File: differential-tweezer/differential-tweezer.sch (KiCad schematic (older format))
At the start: 58 parts, among them J1 5V, J2 IN+, J3 Conn_Coaxial, J4 IN-, J5 Power, U1 R1283B, U2 OPA810, U3 OPA810, U4 OPA810

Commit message: Revision 2
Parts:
- removed C11, C3: 100nF, Capacitor_SMD:C_0603_1608Metric, symbol Device:C
- removed C19: 2pF, Capacitor_SMD:C_0603_1608Metric, symbol Device:C
- removed C23: 6pF, Capacitor_SMD:C_Trimmer_Murata_TZC3, symbol Device:CTRIM
- removed J1: 5V, oscilloscope-probes:WIREPAD_WIDE, symbol Connector:Conn_01x01_Female
- removed J2: IN+, oscilloscope-probes:SOLDERPAD_3x1.5, symbol Connector:Conn_01x01_Female
- removed J3: Conn_Coaxial, oscilloscope-probes:COAX_SOLDER, symbol Connector:Conn_Coaxial
- removed J4: IN-, oscilloscope-probes:SOLDERPAD_3x1.5, symbol Connector:Conn_01x01_Female
- removed J5: Power, Connector_PinHeader_2.54mm:PinHeader_1x04_P2.54mm_Vertical, symbol Connector:Conn_01x04_Male
- removed L3, L5: 1k, Inductor_SMD:L_0603_1608Metric, symbol Device:L_Core_Ferrite
- removed RV1, RV3: 47k, Potentiometer_SMD:Potentiometer_Bourns_TC33X_Vertical, symbol Device:R_POT_TRIM
- removed U2, U3, U4: OPA810, Package_TO_SOT_SMD:SOT-23-5, symbol Amplifier_Operational:OPA842xDBV
- added C1, C26: 10µF, Capacitor_SMD:C_0603_1608Metric, symbol Device:C
- added C10: 100nF, Capacitor_SMD:C_0603_1608Metric, symbol Device:C
- added C14, C15: 20pF, Capacitor_SMD:C_0603_1608Metric, symbol Device:C
- added H1: 2.2mm, MountingHole:MountingHole_2.2mm_M2_DIN965_Pad, symbol Mechanical:MountingHole_Pad
- added J1: Triax, oscilloscope-probes:TRIAX_TUBE, symbol oscilloscope_probes:Conn_Triaxial
- added J2: Input, oscilloscope-probes:Tensility_54-00177, symbol Connector:AudioJack4
- added J3: Probe+, oscilloscope-probes:TE_2306454_RIGHT, symbol Connector_Generic:Conn_01x01
- added J4: Probe+_GND, oscilloscope-probes:TE_2306454_RIGHT, symbol Connector_Generic:Conn_01x01
- added J5: Probe-_GND, oscilloscope-probes:TE_2306454_LEFT, symbol Connector_Generic:Conn_01x01
- added J6: Probe-, oscilloscope-probes:TE_2306454_LEFT, symbol Connector_Generic:Conn_01x01
- added L1, L7, L8: MMZ1608B601, Inductor_SMD:L_0603_1608Metric, symbol Device:L_Core_Ferrite
- added R14, R15: 220, Resistor_SMD:R_0603_1608Metric, symbol Device:R
- added R16, R17: 22, Resistor_SMD:R_0603_1608Metric, symbol Device:R
- added R7: 10M, Resistor_SMD:R_0603_1608Metric, symbol Device:R
- added R9: 499k, Resistor_SMD:R_0603_1608Metric, symbol Device:R
- added RV2: 50k, Potentiometer_SMD:Potentiometer_Bourns_TC33X_Vertical, symbol Device:R_POT_TRIM
- added SW1: GAIN, oscilloscope-probes:78HF01GWRT, symbol Switch:SW_SPST
- added TP1: +5V, TestPoint:TestPoint_Pad_D2.5mm, symbol Connector:TestPoint
- added TP2: +6V, TestPoint:TestPoint_Pad_D2.5mm, symbol Connector:TestPoint
- added TP3: -6V, TestPoint:TestPoint_Pad_D2.5mm, symbol Connector:TestPoint
- added TP4: GND, TestPoint:TestPoint_Pad_D2.5mm, symbol Connector:TestPoint
- added U2, U3, U4: OPA659, Package_SON:Texas_S-PVSON-N8_ThermalVias, symbol oscilloscope_probes:OPA659DRB
- C12: renamed from C4; footprint Capacitor_SMD:C_0805_2012Metric -> Capacitor_SMD:C_0603_1608Metric; Mfg (none) -> AVX; Mfg Part No (none) -> 0603ZD106KAT2A; Notes (none) -> X5R, 10V
- C13: renamed from C12; footprint Capacitor_SMD:C_0805_2012Metric -> Capacitor_SMD:C_0603_1608Metric; Mfg (none) -> AVX; Mfg Part No (none) -> 0603ZD106KAT2A; Notes (none) -> X5R, 10V
- C16: renamed from C20; value 6pF -> 8-30pF; Mfg (none) -> EW; Mfg Part No (none) -> SGC3S300NM
- C17: renamed from C22; value 6pF -> 8-30pF; Mfg (none) -> EW; Mfg Part No (none) -> SGC3S300NM
- C19: renamed from C21; value 2pF -> N/A
- C2: renamed from C16; footprint Capacitor_SMD:C_0805_2012Metric -> Capacitor_SMD:C_0603_1608Metric; Mfg (none) -> AVX; Mfg Part No (none) -> 0603ZD106KAT2A; Notes (none) -> X5R, 10V
- C3: renamed from C17; footprint Capacitor_SMD:C_0805_2012Metric -> Capacitor_SMD:C_0603_1608Metric; Mfg (none) -> AVX; Mfg Part No (none) -> 0603ZD106KAT2A; Notes (none) -> X5R, 10V
- C4: renamed from C8; value 22nF -> 100pF; Mfg (none) -> Stackpole; Mfg Part No (none) -> CML0603C0G101JT50V; Notes (none) -> NP0
- C5: renamed from C18; value 22nF -> 100pF; Mfg (none) -> Stackpole; Mfg Part No (none) -> CML0603C0G101JT50V; Notes (none) -> NP0
- C6: renamed from C1; footprint Capacitor_SMD:C_0805_2012Metric -> Capacitor_SMD:C_0603_1608Metric; Mfg (none) -> AVX; Mfg Part No (none) -> 0603ZD106KAT2A; Notes (none) -> X5R, 10V
- C7: renamed from C9; footprint Capacitor_SMD:C_0805_2012Metric -> Capacitor_SMD:C_0603_1608Metric; Mfg (none) -> AVX; Mfg Part No (none) -> 0603ZD106KAT2A; Notes (none) -> X5R, 10V
- C8: renamed from C2; footprint Capacitor_SMD:C_0805_2012Metric -> Capacitor_SMD:C_0603_1608Metric; Mfg (none) -> AVX; Mfg Part No (none) -> 0603ZD106KAT2A; Notes (none) -> X5R, 10V
- C9: renamed from C10; footprint Capacitor_SMD:C_0805_2012Metric -> Capacitor_SMD:C_0603_1608Metric; Mfg (none) -> AVX; Mfg Part No (none) -> 0603ZD106KAT2A; Notes (none) -> X5R, 10V
- D1: renamed from D2; value BAT54 -> NSR05T30; footprint Diode_SMD:D_SOD-123 -> Diode_SMD:D_SOD-523; Mfg (none) -> ON; Mfg Part No (none) -> NSR05T30XV2T5G
- D2: renamed from D1; value BAT54 -> NSR05T30; footprint Diode_SMD:D_SOD-123 -> Diode_SMD:D_SOD-523; Mfg (none) -> ON; Mfg Part No (none) -> NSR05T30XV2T5G
- L2: renamed from L1; value 1k -> MMZ1608B601; Mfg (none) -> TDK; Mfg Part No (none) -> MMZ1608B601CTAH0; Notes (none) -> Alternative MMZ1608B471
- L3: renamed from L2; value 47µH -> 4.7µH; footprint Inductor_SMD:L_Taiyo-Yuden_NR-40xx_HandSoldering -> Inductor_SMD:L_0805_2012Metric
- L4: renamed from L7; value 47µH -> 4.7µH; footprint Inductor_SMD:L_Taiyo-Yuden_NR-40xx_HandSoldering -> Inductor_SMD:L_0805_2012Metric
- L5: renamed from L4; value 1k -> MMZ1608B601; Mfg (none) -> TDK; Mfg Part No (none) -> MMZ1608B601CTAH0; Notes (none) -> Alternative MMZ1608B471
- L6: value 1k -> MMZ1608B601; Mfg (none) -> TDK; Mfg Part No (none) -> MMZ1608B601CTAH0; Notes (none) -> Alternative MMZ1608B471
- R1: renamed from R6; value 10k -> 1k
- R10: value 1M -> 499k
- R12: renamed from R9; value 1M -> 475k
- R13: renamed from R15; value 1M -> 475k
- R18: renamed from R7; value 470 -> 110
- R19: renamed from R13; value 470 -> 110
- R2: value 100k -> 4.99k
- R20: renamed from R8; value 470 -> 220
- R21: renamed from R14; value 470 -> 220
- R22: renamed from R12; value 47 -> 49.9
- R3: renamed from R5; value 100k -> 4.99k
- R6: renamed from R3; value 10k -> 1k
- RV1: renamed from RV2; value 47k -> 50k; Mfg (none) -> Bourns; Mfg Part No (none) -> TC33X-2-503E
- renumbered C5 to C20, C13 to C21, C6 to C22, C14 to C23, C7 to C24, C15 to C25, R1 to R4, R4 to R5
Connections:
- net GND: now also C1.2, C10.2, C26.2, H1.1, J1.2 (Ext), J2.R2, J2.S, J4.1 (Pin_1), J5.1 (Pin_1), TP4.1; no longer RV1.3
- net IN+: now reaches C16.1, R12.1
- net IN+: now also C14.1, J3.1 (Pin_1), R9.1, U2.3 (+)
- net at R12.2, RV1.1: now also R7.2
- net IN-: now reaches C17.1, R13.1
- net IN-: now also R10.1, C15.1, J6.1 (Pin_1), U3.3 (+)
- net at R13.2: now also RV1.3
- net at R19.1: now also R15.2, U3.6
- net at C19.2, R19.2, R21.1: now also U4.2 (-)
- net at R18.1: now also R14.1, U2.6
- net at R18.2, R20.1: now also U4.3 (+)
- net at C19.1, R21.2, R22.2: now also U4.6
- net CONN_IN-: now reaches R10.2
- net CONN_IN-: now also C15.2, J2.R1; no longer R22.1
- net at C3.1, L2.2, L3.1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: now also C26.1
- net at C6.1, D2.1 (K), R2.1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: now also L5.1
- net at C7.1, D1.2 (A), R3.1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: now also L6.1
- net at C2.1, L2.1: now also L1.2
- net at C9.1: now also L6.2, L8.1; no longer L6.1
- net at C8.1: now also L5.2, L7.1; no longer L5.1
- net +12V renamed +6V
- net +6V: now also L7.2, RV2.1, TP2.1, U2.7 (V+), U3.7 (V+), U4.7 (V+); no longer L5.2
- net -12V renamed -6V
- net -6V: now also L8.2, RV2.3, TP3.1, U2.4 (V-), U2.9 (EP), U3.4 (V-), U3.9 (EP), U4.4 (V-), U4.9 (EP); no longer L6.2
- new net: R15.1, R17.2, U3.2 (-)
- new net: R14.2, R16.2, U2.2 (-)
- new net: R17.1, SW1.1 (A)
- new net: R16.1, SW1.2 (B)
- new net +5V: C1.1, J1.3, L1.1, TP1.1
- new net CONN_IN+: C14.2, J2.T, R9.2
- new net OFFSET_TRIM: C10.1, R7.1, RV2.2
- new net OUT: J1.1 (In), R22.1
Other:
- note added: "C16 and C17 trim input divider compensation.\nRV1 trims low-frequency CMRR.\nRV2 trims input offset voltage."
- note added: "Input has divider resistor and capacitor near the tip to minimize\ncapacitance. For 10x tweezers this is 9.53 Mohm || 1.2 pF.\nThe 3.5 mm input has 1 Mohm || 10 pF input impedance, while\ntweezer connector has 500 kohm || 20 pF."
- note added: "Input protection: OPA659 internal ESD diodes tolerate\nup to 30 mA current. The input divider provides enough\nprotection for any inputs up to the resistor maximum\nvoltage (100 V). The capacitive divider limits ESD events\nto below the 4kV HBM rating of OPA659."
- note added: "Input stage has switchable 1x or 10x amplification.\n\nOutput differential amplifier has 2x amplification ratio.\nR18-R21 should have low thermal drift for good CMMR."
- note removed: "Circuit can be assembled either on 1 PCB with 2-sided SMT,\nor 2 PCBs each with 1-sided SMT."
- note removed: "Probe tip has 9.1Mohm // 0.5pF.\nCombined this forms a 1:10 divider"
- moved on the sheet: C12, C13, C16, C17, C19, C2, C20, C21, C22, C23, C24, C25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

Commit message: Revision 3
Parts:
- removed C14, C15: 20pF, Capacitor_SMD:C_0603_1608Metric, symbol Device:C
- removed J1: Triax, oscilloscope-probes:TRIAX_TUBE, symbol oscilloscope_probes:Conn_Triaxial
- removed J2: Input, oscilloscope-probes:Tensility_54-00177, symbol Connector:AudioJack4
- removed R4, R5: 1k, Resistor_SMD:R_0603_1608Metric, symbol Device:R
- added C11: 3pF, Capacitor_SMD:C_0603_1608Metric, symbol Device:C
- added D3: RED, LED_SMD:LED_0603_1608Metric, symbol Device:LED_ALT
- added D4, D5, D6: PESD5V0X1B, Package_TO_SOT_SMD:SOT-23, symbol Device:D_Zener_x2_ACom_KKA
- added J1: Triax_inner, oscilloscope-probes:COAX_2MM, symbol Connector:Conn_Coaxial
- added J2: Triax_outer, oscilloscope-probes:TRIAX_OUTER_3MM, symbol Connector_Generic:Conn_01x01
- added J7: IN+, oscilloscope-probes:RF11-27A-T-00-50-G, symbol Connector:Conn_Coaxial
- added J8: IN-, oscilloscope-probes:RF11-27A-T-00-50-G, symbol Connector:Conn_Coaxial
- added L9: MMZ1608B601, Inductor_SMD:L_0603_1608Metric, symbol Device:L_Core_Ferrite
- added R11, R23: 110, Resistor_SMD:R_0603_1608Metric, symbol Device:R
- added R8: 5.1k, Resistor_SMD:R_0603_1608Metric, symbol Device:R
- C1: value 10µF -> 3pF
- C19: value N/A -> 3pF
- J3: value Probe+ -> Spring+S
- J4: value Probe+_GND -> Spring+G
- J5: value Probe-_GND -> Spring-G
- J6: value Probe- -> Spring-S
- L3, L4: footprint Inductor_SMD:L_0805_2012Metric -> Inductor_SMD:L_0805_2012Metric_Pad1.15x1.40mm_HandSolder; Mfg (none) -> TDK; Mfg Part No (none) -> MLZ2012N4R7LT000
- R10, R9: value 499k -> 49.9
- R12, R13: value 475k -> 487k
- R14, R15, R20, R21: Mfg (none) -> Panasonic; Mfg Part No (none) -> ERA-3AED221V; Notes (none) -> 0.5%, 25ppm/K
- R16, R17: value 22 -> 24
- R18, R19: Mfg (none) -> Panasonic; Mfg Part No (none) -> ERA-3AED111V; Notes (none) -> 0.5%, 25ppm/K
- R2, R3: value 4.99k -> 5.1k
- R7: value 10M -> 5.1k
- RV1, RV2: value 50k -> 20k
- SW1: Mfg C&K -> Grayhill; Mfg Part No JS202011JCQN -> 78HF01GWRT
- U1: value R1283B -> R1283K001C
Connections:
- net +5V: now also J2.1 (Pin_1); no longer C1.1
- net +6V: now also R8.2
- net CONN_IN+: now also J7.1 (In)
- net CONN_IN-: now also J8.1 (In)
- net GND: now also L9.2; no longer C1.2, C10.2, C12.2, C13.2, C16.2, C17.2, C20.2, C21.1, C22.2, C23.1, C24.2, C25.1, H1.1, J4.1 (Pin_1), J5.1 (Pin_1), R20.2, RV1.2, TP4.1
- net IN+: now also D4.1 (K), R23.2; no longer U2.3 (+)
- net IN-: now also D5.2 (K), R11.2; no longer U3.3 (+)
- net OUT: now also R7.2, D6.1 (K), J1.1 (In)
- net at R12.2, RV1.1: no longer R7.2
- net at R15.2, R19.1, U3.6: now also C11.1
- net at R14.1, R18.1, U2.6: now also C1.2
- net at C6.1, D2.1 (K), L5.1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: now also C4.1
- net at C5.1: now also C7.1, D1.2 (A), L6.1, R3.1
- net at R15.1, U3.2 (-): now also R17.1, C11.2; no longer R17.2
- net at R14.2, U2.2 (-): now also C1.1, R16.1; no longer R16.2
- net at SW1.1 (A): now also R17.2; no longer R17.1
- net at SW1.2 (B): now also R16.2; no longer R16.1
- new net: D3.2 (A), R8.1
- new net: R23.1, U2.3 (+)
- new net: R11.1, U3.3 (+)
- new net GNDA: C10.2, C12.2, C13.2, C16.2, C17.2, C20.2, C21.1, C22.2, C23.1, C24.2, C25.1, D3.1 (K), D4.2 (K), D5.1 (K), D6.2 (K), H1.1, J1.2 (Ext), J4.1 (Pin_1), J5.1 (Pin_1), J7.2 (Ext), J8.2 (Ext), L9.1, R20.2, RV1.2, TP4.1
- no-connect marks 1 -> 4
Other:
- note added: "Input protection: OPA659 internal ESD diodes tolerate\nup to 30 mA current. D4 and D5 clamp to about 9V and\nthe 110 ohm resistors limit the current that flows to\nopamp input pins. Input maximum DC voltage is limited\nby the power handling of the 49.9 ohm resistors to 12V.\n\nFurther protection is provided by the larger series resistors\nin the probe tips, which will protect up to their maximum 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"
- note added: "Input stage has switchable 1x or 10x amplification.\n\nOutput differential amplifier has 2x amplification ratio.\nR18-R21 should have low thermal drift for good CMRR."
- note added: "Probe tips have divider resistor and capacitor near the tip to minimize\ncapacitance. For 10x tweezers this is 9.53 Mohm || 1.2 pF.\nThe input impedance is 500 kohm || 10-30 pF.\nInput voltage range is +-3 V."
- note added: "Split ground plane keeps SMPS current spikes from\ninducing noise voltages to measurement circuit.\nPlane crossings are through ferrites."
- note removed: "Input has divider resistor and capacitor near the tip to minimize\ncapacitance. For 10x tweezers this is 9.53 Mohm || 1.2 pF.\nThe 3.5 mm input has 1 Mohm || 10 pF input impedance, while\ntweezer connector has 500 kohm || 20 pF."
- note removed: "Input protection: OPA659 internal ESD diodes tolerate\nup to 30 mA current. The input divider provides enough\nprotection for any inputs up to the resistor maximum\nvoltage (100 V). The capacitive divider limits ESD events\nto below the 4kV HBM rating of OPA659."
- note removed: "Input stage has switchable 1x or 10x amplification.\n\nOutput differential amplifier has 2x amplification ratio.\nR18-R21 should have low thermal drift for good CMMR."
- moved on the sheet: C10, C22, C23, C24, C25, C4, C5, D1, J3, J4, J5, J6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

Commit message: BOM updates
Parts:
- added C18: 6pF, Capacitor_SMD:C_0603_1608Metric, symbol Device:C
- C1, C11, C19: value 3pF -> 6pF
- C4, C5: value 100pF -> 68pF
- J1: Mfg (none) -> WE; Mfg Part No (none) -> 970050244
- J2: Mfg (none) -> WE; Mfg Part No (none) -> 970050354
- J7, J8: Mfg (none) -> Adam Tech; Mfg Part No (none) -> RF11-27A-T-00-50-G
- L1, L2, L5, L6, L7, L8, L9: Mfg TDK -> (none); Mfg Part No MMZ1608B601CTAH0 -> (none); Notes Alternative MMZ1608B471 -> (none)
- L3, L4: Mfg TDK -> Murata; Mfg Part No MLZ2012N4R7LT000 -> DFE201612E-4R7M=P2
- RV1, RV2: value 20k -> 30k; Mfg Part No TC33X-2-503E -> TC33X-2-303E
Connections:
- net GNDA: now also C18.1
- net at R18.2, R20.1, U4.3 (+): now also C18.2
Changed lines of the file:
@@
 P 7500 6200
 F 0 "C19" V 7660 6200 50  0000 C CNN
-F 1 "3pF" V 7751 6200 50  0000 C CNN
+F 1 "6pF" V 7751 6200 50  0000 C CNN
 F 2 "Capacitor_SMD:C_0603_1608Metric" H 7538 6050 50  0001 C CNN
 F 3 "~" H 7500 6200 50  0001 C CNN
@@
 U 1 1 5FFD20E6
 P 7500 4200
-F 0 "R20" V 7707 4200 50  0000 C CNN
-F 1 "220" V 7616 4200 50  0000 C CNN
+F 0 "R20" V 7385 4200 50  0000 C CNN
+F 1 "220" V 7294 4200 50  0000 C CNN
 F 2 "Resistor_SMD:R_0603_1608Metric" V 7430 4200 50  0001 C CNN
 F 3 "~" H 7500 4200 50  0001 C CNN
@@
 P 4300 5050
 F 0 "RV1" H 4230 5096 50  0000 R CNN
-F 1 "20k" H 4230 5005 50  0000 R CNN
+F 1 "30k" H 4230 5005 50  0000 R CNN
 F 2 "Potentiometer_SMD:Potentiometer_Bourns_TC33X_Vertical" H 4300 5050 50  0001 C CNN
 F 3 "~" H 4300 5050 50  0001 C CNN
 F 4 "Bourns" H 4300 5050 50  0001 C CNN "Mfg"
-F 5 "TC33X-2-503E" H 4300 5050 50  0001 C CNN "Mfg Part No"
+F 5 "TC33X-2-303E" H 4300 5050 50  0001 C CNN "Mfg Part No"
 	1    4300 5050
 	-1   0    0    -1
@@
 F 2 "Inductor_SMD:L_0805_2012Metric_Pad1.15x1.40mm_HandSolder" H 4650 900 50  0001 C CNN
 F 3 "~" H 4650 900 50  0001 C CNN
-F 4 "TDK" H 4650 900 50  0001 C CNN "Mfg"
-F 5 "MLZ2012N4R7LT000" H 4650 900 50  0001 C CNN "Mfg Part No"
+F 4 "Murata" H 4650 900 50  0001 C CNN "Mfg"
+F 5 "DFE201612E-4R7M=P2" H 4650 900 50  0001 C CNN "Mfg Part No"
 	1    4650 900
 	0    -1   -1   0
@@
 P 6000 2150
 F 0 "C5" H 6115 2196 50  0000 L CNN
-F 1 "100pF" H 6115 2105 50  0000 L CNN
+F 1 "68pF" H 6115 2105 50  0000 L CNN
 F 2 "Capacitor_SMD:C_0603_1608Metric" H 6038 2000 50  0001 C CNN
 F 3 "~" H 6000 2150 50  0001 C CNN
@@
 F 2 "Inductor_SMD:L_0805_2012Metric_Pad1.15x1.40mm_HandSolder" H 4900 2000 50  0001 C CNN
 F 3 "~" H 4900 2000 50  0001 C CNN
-F 4 "TDK" H 4900 2000 50  0001 C CNN "Mfg"
-F 5 "MLZ2012N4R7LT000" H 4900 2000 50  0001 C CNN "Mfg Part No"
+F 4 "Murata" H 4900 2000 50  0001 C CNN "Mfg"
+F 5 "DFE201612E-4R7M=P2" H 4900 2000 50  0001 C CNN "Mfg Part No"
 	1    4900 2000
 	0    1    1    0
@@
 F 2 "Inductor_SMD:L_0603_1608Metric" H 2700 900 50  0001 C CNN
 F 3 "~" H 2700 900 50  0001 C CNN
-F 4 "TDK" H 2700 900 50  0001 C CNN "Mfg"
-F 5 "MMZ1608B601CTAH0" H 2700 900 50  0001 C CNN "Mfg Part No"
-F 6 "Alternative MMZ1608B471" H 2700 900 50  0001 C CNN "Notes"
+F 4 "" H 2700 900 50  0001 C CNN "Mfg"
+F 5 "" H 2700 900 50  0001 C CNN "Mfg Part No"
+F 6 "" H 2700 900 50  0001 C CNN "Notes"
 	1    2700 900
 	0    -1   -1   0
@@
 F 2 "Inductor_SMD:L_0603_1608Metric" H 7400 1800 50  0001 C CNN
 F 3 "~" H 7400 1800 50  0001 C CNN
-F 4 "TDK" H 7400 1800 50  0001 C CNN "Mfg"
-F 5 "MMZ1608B601CTAH0" H 7400 1800 50  0001 C CNN "Mfg Part No"
-F 6 "Alternative MMZ1608B471" H 7400 1800 50  0001 C CNN "Notes"
+F 4 "" H 7400 1800 50  0001 C CNN "Mfg"
+F 5 "" H 7400 1800 50  0001 C CNN "Mfg Part No"
+F 6 "" H 7400 1800 50  0001 C CNN "Notes"
 	1    7400 1800
 	0    -1   -1   0
@@
 F 2 "Inductor_SMD:L_0603_1608Metric" H 7400 900 50  0001 C CNN
 F 3 "~" H 7400 900 50  0001 C CNN
-F 4 "TDK" H 7400 900 50  0001 C CNN "Mfg"
-F 5 "MMZ1608B601CTAH0" H 7400 900 50  0001 C CNN "Mfg Part No"
-F 6 "Alternative MMZ1608B471" H 7400 900 50  0001 C CNN "Notes"
+F 4 "" H 7400 900 50  0001 C CNN "Mfg"
+F 5 "" H 7400 900 50  0001 C CNN "Mfg Part No"
+F 6 "" H 7400 900 50  0001 C CNN "Notes"
 	1    7400 900
 	0    -1   -1   0
@@
 P 6000 1200
 F 0 "C4" H 6115 1246 50  0000 L CNN
-F 1 "100pF" H 6115 1155 50  0000 L CNN
+F 1 "68pF" H 6115 1155 50  0000 L CNN
 F 2 "Capacitor_SMD:C_0603_1608Metric" H 6038 1050 50  0001 C CNN
 F 3 "~" H 6000 1200 50  0001 C CNN
@@
 P 8400 5650
 F 0 "RV2" H 8330 5696 50  0000 R CNN
-F 1 "20k" H 8330 5605 50  0000 R CNN
+F 1 "30k" H 8330 5605 50  0000 R CNN
 F 2 "Potentiometer_SMD:Potentiometer_Bourns_TC33X_Vertical" H 8400 5650 50  0001 C CNN
 F 3 "~" H 8400 5650 50  0001 C CNN
 F 4 "Bourns" H 8400 5650 50  0001 C CNN "Mfg"
-F 5 "TC33X-2-503E" H 8400 5650 50  0001 C CNN "Mfg Part No"
+F 5 "TC33X-2-303E" H 8400 5650 50  0001 C CNN "Mfg Part No"
 	1    8400 5650
 	1    0    0    -1
@@
 	2850 900  3150 900
 Connection ~ 3150 900
-Text Notes 2700 3750 0    50   ~ 0
+Text Notes 2400 3500 0    50   ~ 0
 C16 and C17 trim input divider compensation.\nRV1 trims low-frequency CMRR.\nRV2 trims input offset voltage.
 $Comp
@@
 F 2 "Inductor_SMD:L_0603_1608Metric" H 1850 900 50  0001 C CNN
 F 3 "~" H 1850 900 50  0001 C CNN
-F 4 "TDK" H 1850 900 50  0001 C CNN "Mfg"
-F 5 "MMZ1608B601CTAH0" H 1850 900 50  0001 C CNN "Mfg Part No"
-F 6 "Alternative MMZ1608B471" H 1850 900 50  0001 C CNN "Notes"
+F 4 "" H 1850 900 50  0001 C CNN "Mfg"
+F 5 "" H 1850 900 50  0001 C CNN "Mfg Part No"
+F 6 "" H 1850 900 50  0001 C CNN "Notes"
 	1    1850 900
 	0    -1   -1   0
@@
 F 2 "Inductor_SMD:L_0603_1608Metric" H 8250 1800 50  0001 C CNN
 F 3 "~" H 8250 1800 50  0001 C CNN
-F 4 "TDK" H 8250 1800 50  0001 C CNN "Mfg"
-F 5 "MMZ1608B601CTAH0" H 8250 1800 50  0001 C CNN "Mfg Part No"
-F 6 "Alternative MMZ1608B471" H 8250 1800 50  0001 C CNN "Notes"
+F 4 "" H 8250 1800 50  0001 C CNN "Mfg"
+F 5 "" H 8250 1800 50  0001 C CNN "Mfg Part No"
+F 6 "" H 8250 1800 50  0001 C CNN "Notes"
 	1    8250 1800
 	0    -1   -1   0
@@
 F 2 "Inductor_SMD:L_0603_1608Metric" H 8250 900 50  0001 C CNN
 F 3 "~" H 8250 900 50  0001 C CNN
-F 4 "TDK" H 8250 900 50  0001 C CNN "Mfg"
-F 5 "MMZ1608B601CTAH0" H 8250 900 50  0001 C CNN "Mfg Part No"
-F 6 "Alternative MMZ1608B471" H 8250 900 50  0001 C CNN "Notes"
+F 4 "" H 8250 900 50  0001 C CNN "Mfg"
+F 5 "" H 8250 900 50  0001 C CNN "Mfg Part No"
+F 6 "" H 8250 900 50  0001 C CNN "Notes"
 	1    8250 900
 	0    -1   -1   0
@@
 	1    0    0    1
 $EndComp
-Text Notes 6100 3800 0    50   ~ 0
+Text Notes 5000 3600 0    50   ~ 0
 Input stage has switchable 1x or 10x amplification.\n\nOutput differential amplifier has 2x amplification ratio.\nR18-R21 should have low thermal drift for good CMRR.
 Text Notes 1100 7450 0    50   ~ 0
@@
 F 2 "Inductor_SMD:L_0603_1608Metric" H 1850 2650 50  0001 C CNN
 F 3 "~" H 1850 2650 50  0001 C CNN
-F 4 "TDK" H 1850 2650 50  0001 C CNN "Mfg"
-F 5 "MMZ1608B601CTAH0" H 1850 2650 50  0001 C CNN "Mfg Part No"
-F 6 "Alternative MMZ1608B471" H 1850 2650 50  0001 C CNN "Notes"
+F 4 "" H 1850 2650 50  0001 C CNN "Mfg"
+F 5 "" H 1850 2650 50  0001 C CNN "Mfg Part No"
+F 6 "" H 1850 2650 50  0001 C CNN "Notes"
 	1    1850 2650
 	0    -1   -1   0
@@
 P 6250 5700
 F 0 "C11" H 6135 5654 50  0000 R CNN
-F 1 "3pF" H 6135 5745 50  0000 R CNN
+F 1 "6pF" H 6135 5745 50  0000 R CNN
 F 2 "Capacitor_SMD:C_0603_1608Metric" H 6288 5550 50  0001 C CNN
 F 3 "~" H 6250 5700 50  0001 C CNN
@@
 P 6250 4450
 F 0 "C1" H 6135 4404 50  0000 R CNN
-F 1 "3pF" H 6135 4495 50  0000 R CNN
+F 1 "6pF" H 6135 4495 50  0000 R CNN
 F 2 "Capacitor_SMD:C_0603_1608Metric" H 6288 4300 50  0001 C CNN
 F 3 "~" H 6250 4450 50  0001 C CNN
@@
 F 2 "oscilloscope-probes:COAX_2MM" H 10550 5100 50  0001 C CNN
 F 3 " ~" H 10550 5100 50  0001 C CNN
+F 4 "WE" H 10550 5100 50  0001 C CNN "Mfg"
+F 5 "970050244" H 10550 5100 50  0001 C CNN "Mfg Part No"
 	1    10550 5100
 	1    0    0    -1
@@
 F 2 "oscilloscope-probes:RF11-27A-T-00-50-G" H 950 4100 50  0001 C CNN
 F 3 " ~" H 950 4100 50  0001 C CNN
+F 4 "Adam Tech" H 950 4100 50  0001 C CNN "Mfg"
+F 5 "RF11-27A-T-00-50-G" H 950 4100 50  0001 C CNN "Mfg Part No"
 	1    950  4100
 	-1   0    0    -1
@@
 F 2 "oscilloscope-probes:RF11-27A-T-00-50-G" H 950 5900 50  0001 C CNN
 F 3 " ~" H 950 5900 50  0001 C CNN
+F 4 "Adam Tech" H 950 5900 50  0001 C CNN "Mfg"
+F 5 "RF11-27A-T-00-50-G" H 950 5900 50  0001 C CNN "Mfg Part No"
 	1    950  5900
 	-1   0    0    1
@@
 F 2 "oscilloscope-probes:TRIAX_OUTER_3MM" H 10550 4900 50  0001 C CNN
 F 3 "~" H 10550 4900 50  0001 C CNN
+F 4 "WE" H 10550 4900 50  0001 C CNN "Mfg"
+F 5 "970050354" H 10550 4900 50  0001 C CNN "Mfg Part No"
 	1    10550 4900
 	0    1    1    0
@@
 Connection ~ 8800 3950
 Connection ~ 8800 4250
+$Comp
+L Device:C C18
+U 1 1 60BF3058
+P 7500 4000
+F 0 "C18" V 7248 4000 50  0000 C CNN
+F 1 "6pF" V 7339 4000 50  0000 C CNN
+F 2 "Capacitor_SMD:C_0603_1608Metric" H 7538 3850 50  0001 C CNN
+F 3 "~" H 7500 4000 50  0001 C CNN
+	1    7500 4000
+	0    1    1    0
+$EndComp
+Wire Wire Line
+	7350 4000 6950 4000
+Wire Wire Line
+	6950 4000 6950 4200
+Wire Wire Line
+	7650 4000 8050 4000
+Wire Wire Line
+	8050 4000 8050 4200
+Connection ~ 8050 4200
 $EndSCHEMATC

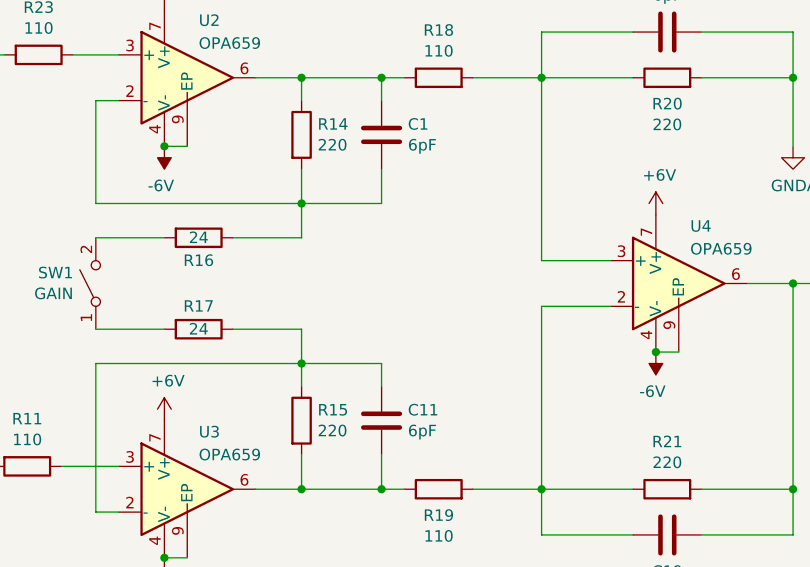
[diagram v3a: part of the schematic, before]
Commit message: Beginnings of manual
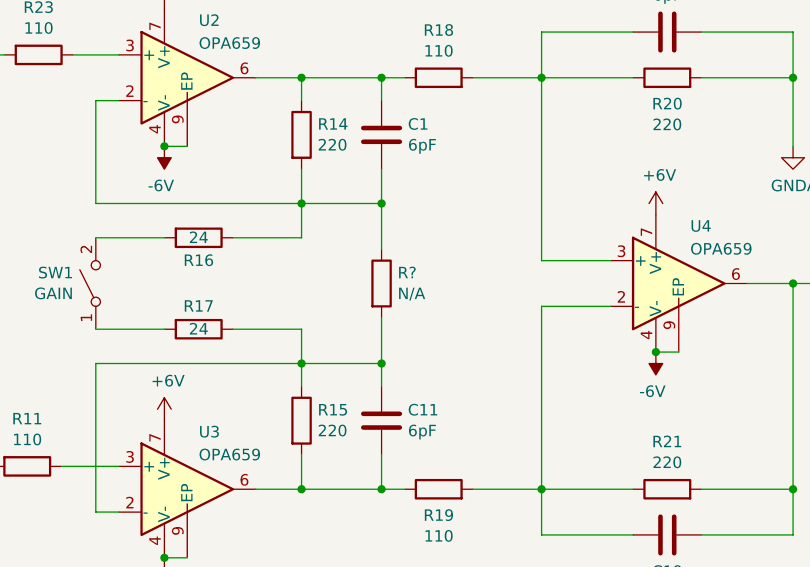
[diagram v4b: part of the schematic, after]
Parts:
- added R?: N/A, Resistor_SMD:R_0603_1608Metric, symbol Device:R
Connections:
- net at C11.2, R15.1, R17.1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: now also R?.2
- net at C1.1, R14.2, R16.1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: now also R?.1
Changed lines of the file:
@@
 	8050 4000 8050 4200
 Connection ~ 8050 4200
+$Comp
+L Device:R R?
+U 1 1 614293EE
+P 6250 5100
+F 0 "R?" H 6320 5146 50  0000 L CNN
+F 1 "N/A" H 6320 5055 50  0000 L CNN
+F 2 "Resistor_SMD:R_0603_1608Metric" V 6180 5100 50  0001 C CNN
+F 3 "~" H 6250 5100 50  0001 C CNN
+F 4 "Panasonic" H 6250 5100 50  0001 C CNN "Mfg"
+F 5 "ERA-3AED111V" H 6250 5100 50  0001 C CNN "Mfg Part No"
+F 6 "0.5%, 25ppm/K" H 6250 5100 50  0001 C CNN "Notes"
+	1    6250 5100
+	1    0    0    -1
+$EndComp
+Wire Wire Line
+	6250 4950 6250 4750
+Connection ~ 6250 4750
+Wire Wire Line
+	6250 5250 6250 5450
+Connection ~ 6250 5450
 $EndSCHEMATC
